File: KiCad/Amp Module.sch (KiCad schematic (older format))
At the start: 59 parts, among them J1 IDC34, J2 IDC34, J3 IDC34, Q1 S9012, Q2 S9012, Q3 S9012, Q4 S9012, SW1 SPDT, SW2 SPDT, U1 74LS08, U2 74LS08, U3 CD4053B, U4 LM393, U5 LM393, U6 LM393, U7 LM393, U8 LM393

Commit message: first 2way commit
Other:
- note added: "v2"
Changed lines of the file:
@@
 Wire Wire Line
 	8650 4700 8500 4700
+Text Notes 7650 6200 0    50   ~ 0
+v2
 $EndSCHEMATC

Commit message: added basic filter and trim
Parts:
- removed R1, R11, R3, R9: ?, symbol Device:R_Small
- removed R12, R13, R4, R5: 12k, symbol Device:R_Small
- removed RV1, RV2: 100k, symbol Device:R_POT_Dual
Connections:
- wire segments 215 -> 185
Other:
- note removed: "VOLUME CONTROL"
- note removed: "v2"

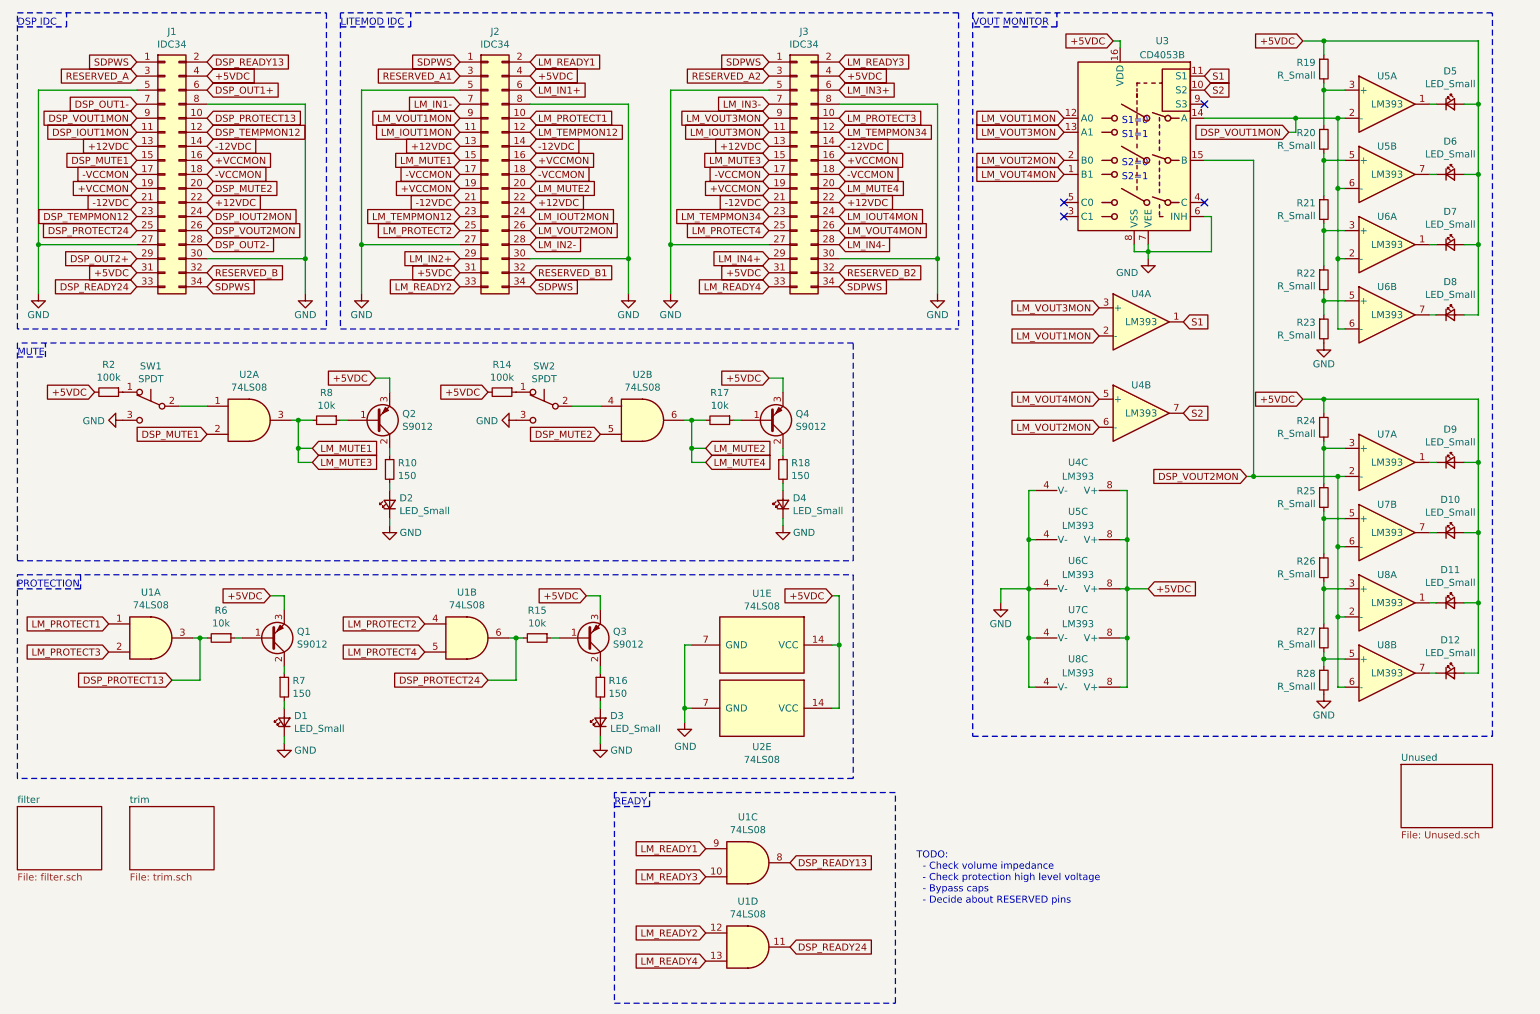
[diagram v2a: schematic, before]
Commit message: restored filter and added initial attenuation in trim
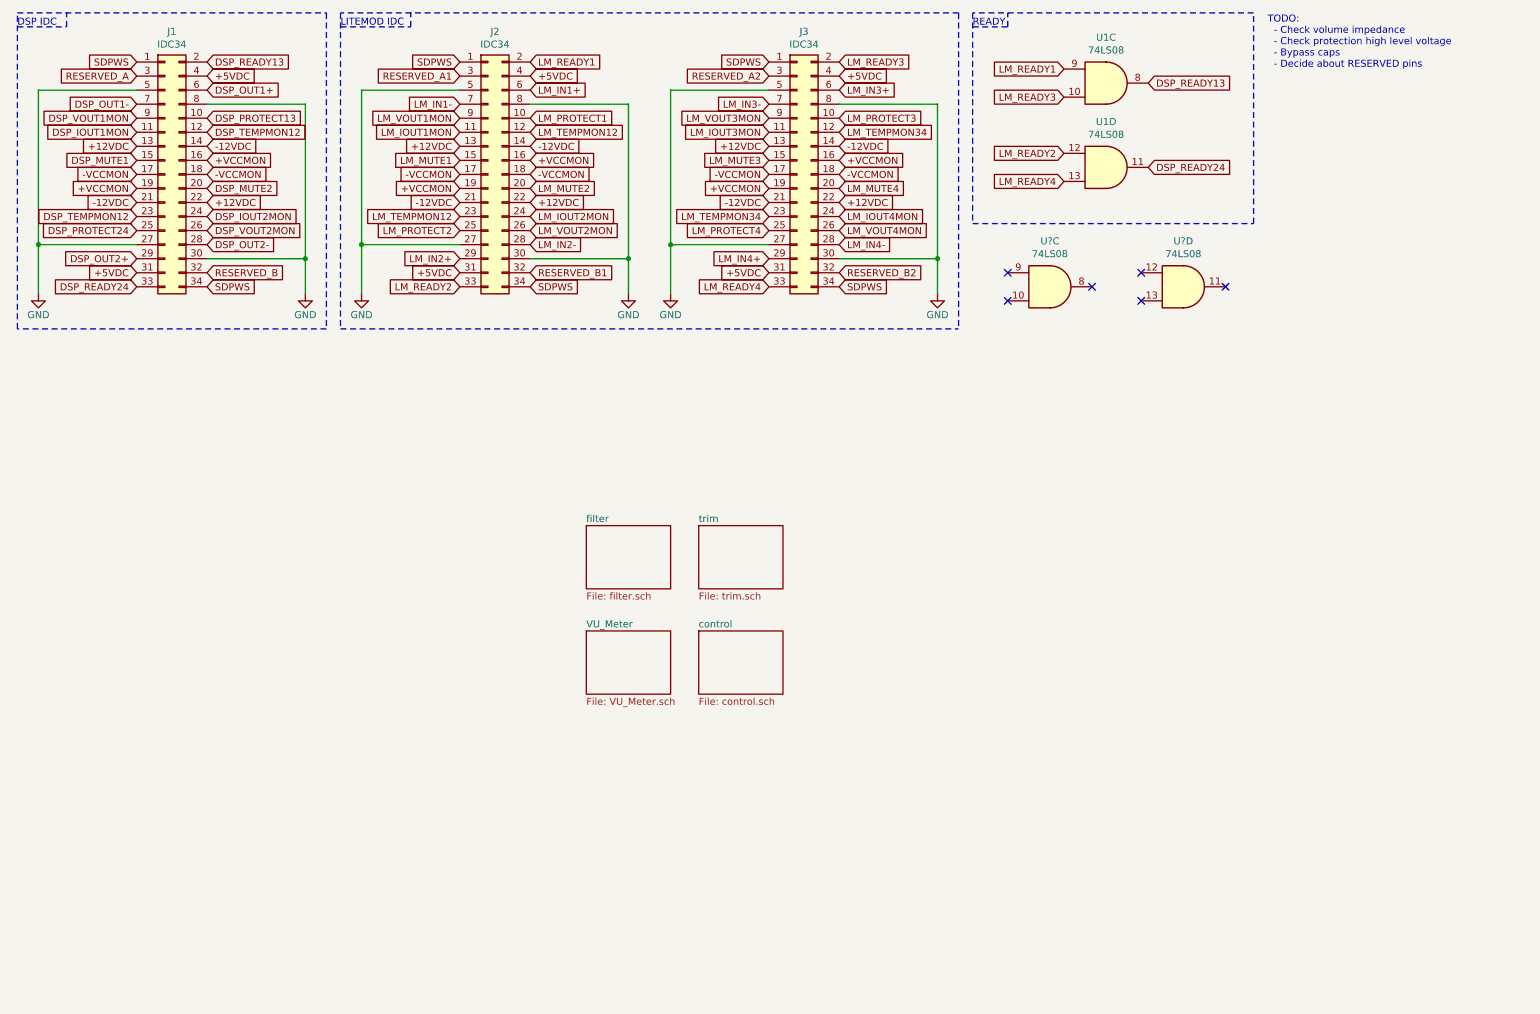
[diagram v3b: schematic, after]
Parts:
- removed D1, D10, D11, D12, D2, D3, D4, D5, D6, D7, D8, D9: LED_Small, symbol Device:LED_Small
- removed Q1, Q2, Q3, Q4: S9012, symbol Device:Q_PNP_BCE
- removed R10, R16, R18, R7: 150, symbol Device:R_Small
- removed R14, R2: 100k, symbol Device:R_Small
- removed R15, R17, R6, R8: 10k, symbol Device:R_Small
- removed R19, R20, R21, R22, R23, R24, R25, R26, R27, R28: R_Small, symbol Device:R_Small
- removed SW1, SW2: SPDT, symbol Switch:SW_Push_SPDT
- removed unit 1 of U1
- removed unit 2 of U1
- removed unit 5 of U1
- removed U2: 74LS08, symbol 74xx:74LS08
- removed U3: CD4053B, symbol Analog_Switch:CD4053B
- removed U4, U5, U6, U7, U8: LM393, symbol Comparator:LM393
- added U? (x2): 74LS08, symbol 74xx:74LS08
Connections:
- net LM_MUTE1: no longer J3.15 (Pin_15)
- net LM_MUTE2: no longer J3.20 (Pin_20)
- new net LM_MUTE3: J3.15 (Pin_15)
- new net LM_MUTE4: J3.20 (Pin_20)
- no-connect marks 4 -> 6
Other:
- note removed: "MUTE"
- note removed: "PROTECTION"
- note removed: "S1=0"
- note removed: "S1=1"
- note removed: "S2=0"
- note removed: "S2=1"
- note removed: "VOUT MONITOR"
- moved on the sheet: U1C, U1D

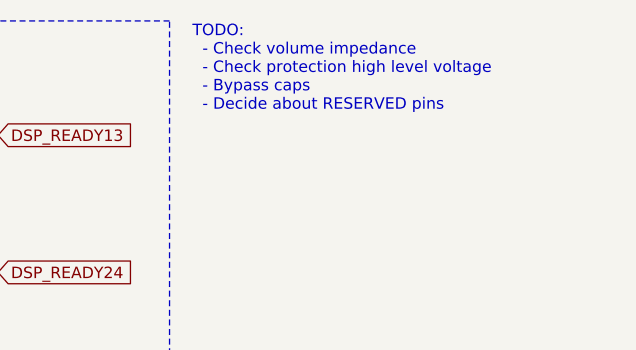
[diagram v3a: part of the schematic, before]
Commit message: changed Q to a fixed value
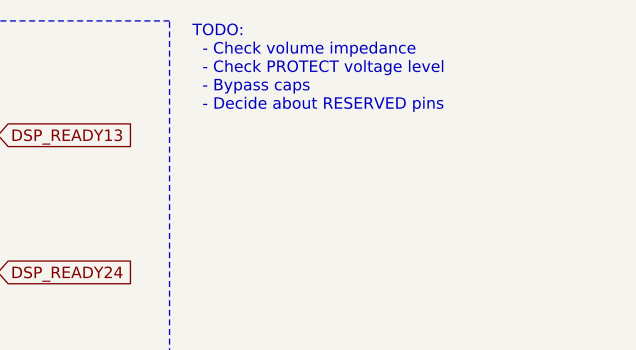
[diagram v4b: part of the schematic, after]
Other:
- note added: "TODO:\n - Check volume impedance\n - Check PROTECT voltage level\n - Bypass caps\n - Decide about RESERVED pins"
- note removed: "TODO:\n - Check volume impedance\n - Check protection high level voltage\n - Bypass caps\n - Decide about RESERVED pins"
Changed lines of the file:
@@
 $EndComp
 Text Notes 9500 1000 0    50   ~ 0
-TODO:\n  - Check volume impedance\n  - Check protection high level voltage\n  - Bypass caps\n  - Decide about RESERVED pins
+TODO:\n  - Check volume impedance\n  - Check PROTECT voltage level\n  - Bypass caps\n  - Decide about RESERVED pins
 Wire Notes Line
 	7400 600  7400 2100

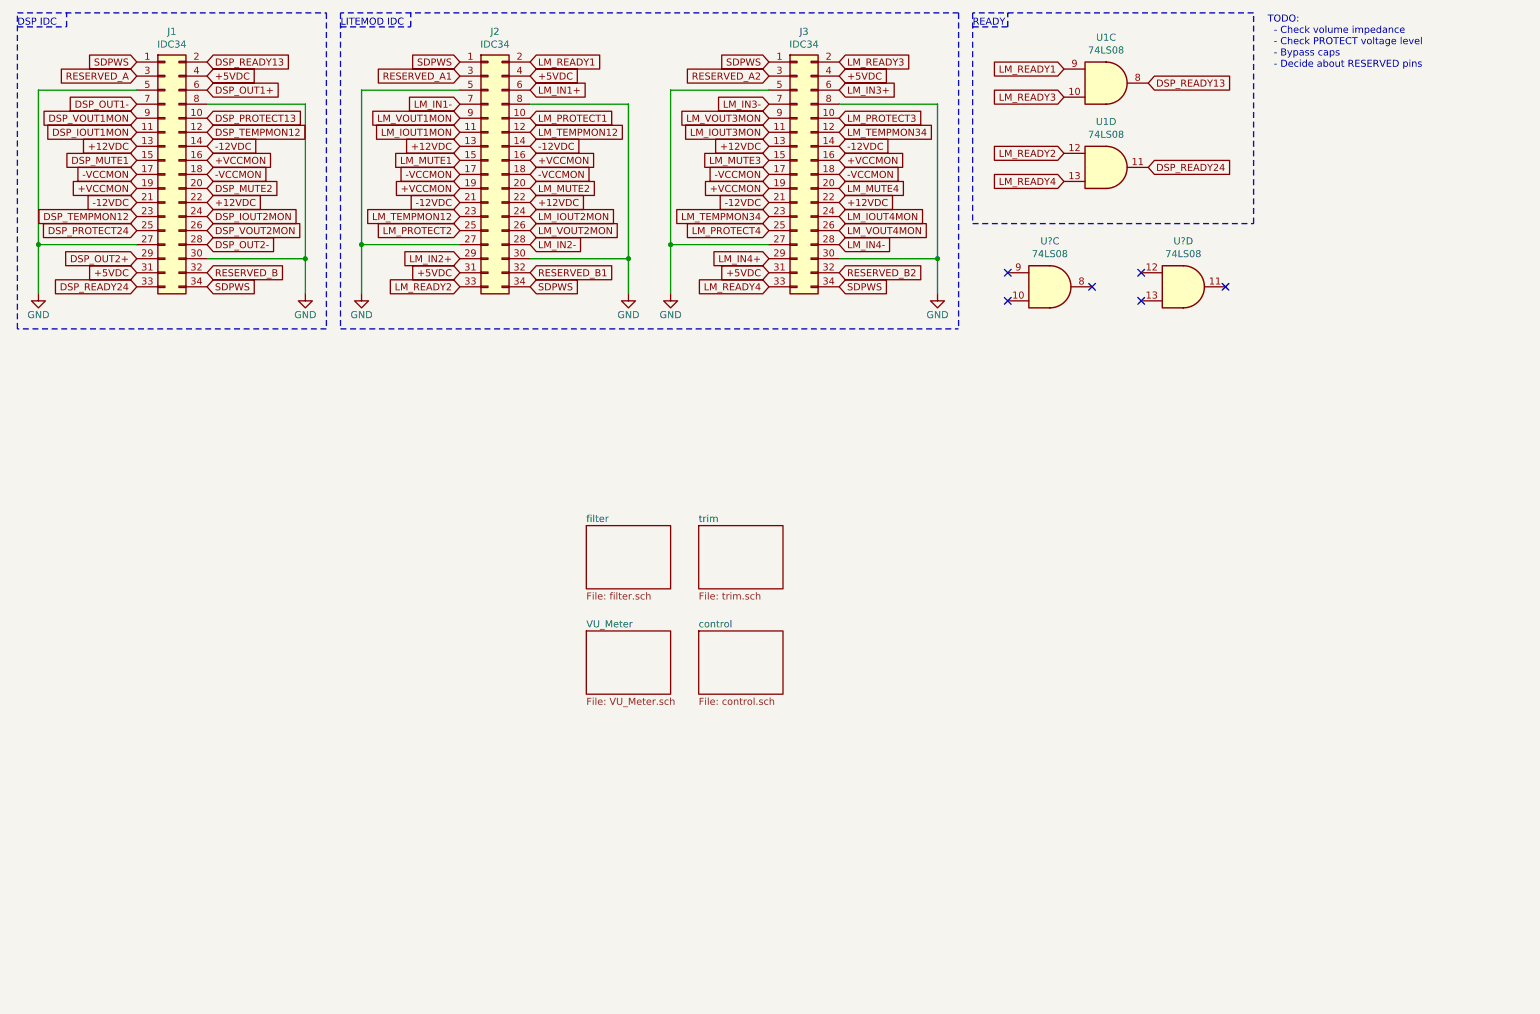
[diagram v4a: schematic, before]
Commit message: removed VU Meter sheet
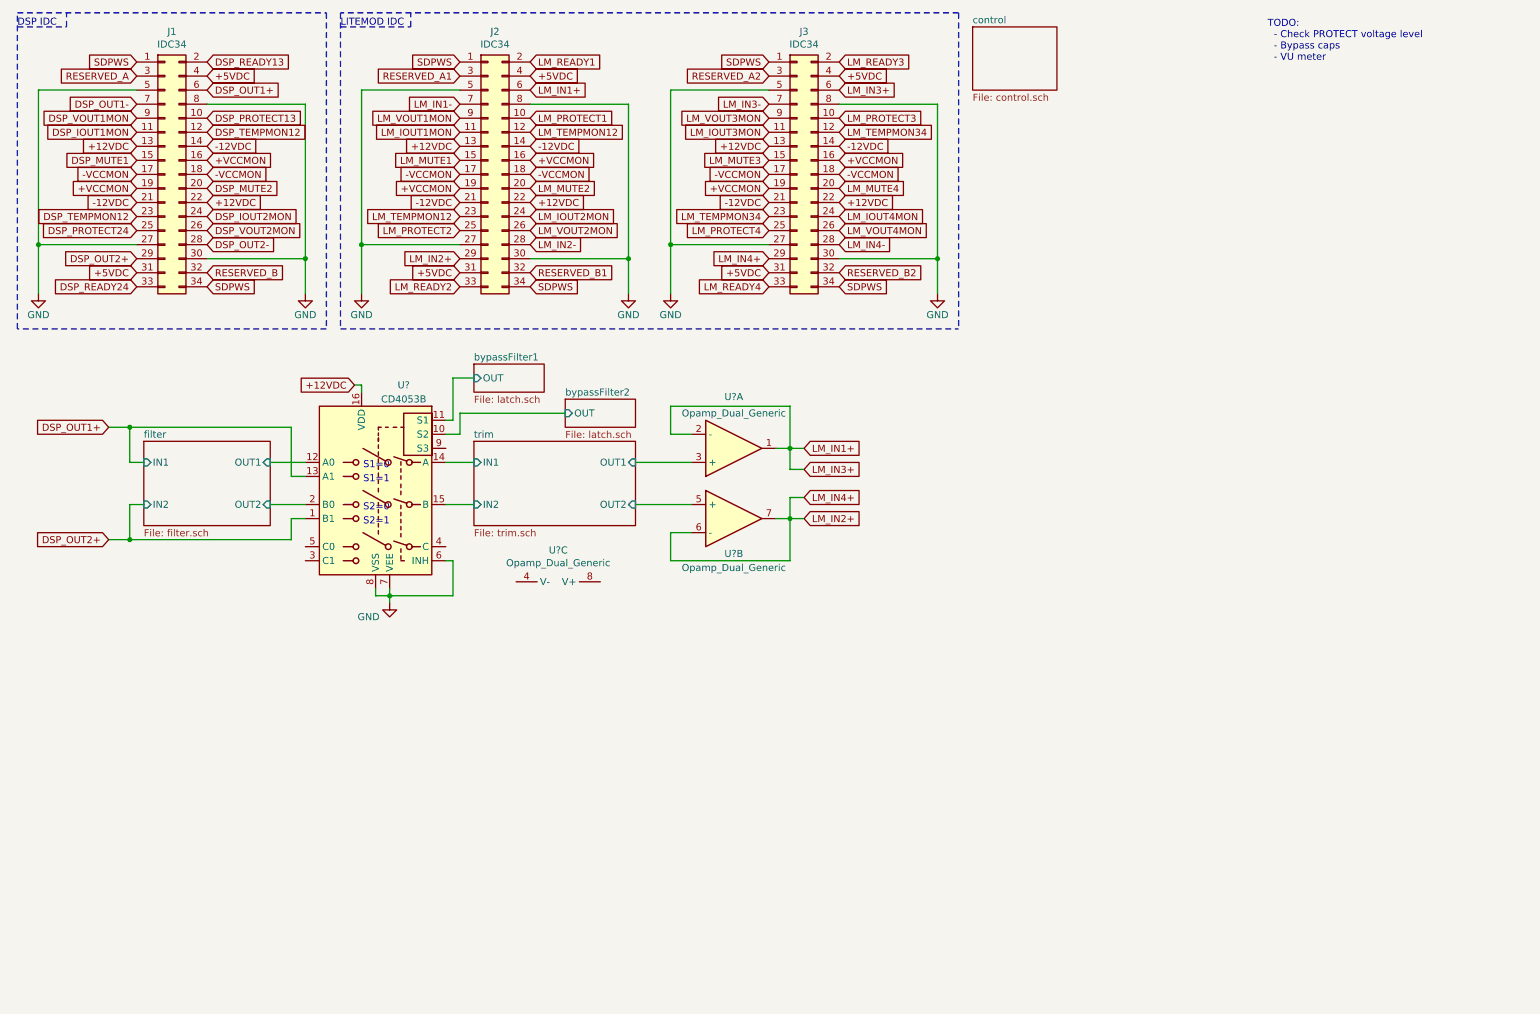
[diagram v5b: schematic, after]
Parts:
- removed U1, U? (x2): 74LS08, symbol 74xx:74LS08
- added U? (x3): Opamp_Dual_Generic, symbol Device:Opamp_Dual_Generic
- added U?: CD4053B, symbol Analog_Switch:CD4053B
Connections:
- net LM_IN3+ is gone; now on net LM_IN1+: J3.6 (Pin_6)
- net LM_IN4+ is gone; now on net LM_IN2+: J3.29 (Pin_29)
- net +12VDC: now also U?.16 (VDD)
- net DSP_OUT1+: now also U?.13 (A1)
- net DSP_OUT2+: now also U?.1 (B1)
- net GND: now also U?.6 (INH), U?.7 (VEE), U?.8 (VSS)
- net LM_IN1+: now also U?.1, U?.2 (-)
- net LM_IN2+: now also U?.6 (-), U?.7
- new net bypassFilter1/OUT: U?.11 (S1)
- new net bypassFilter2/OUT: U?.10 (S2)
- new net filter/OUT1: U?.12 (A0)
- new net filter/OUT2: U?.2 (B0)
- new net trim/IN1: U?.14 (A)
- new net trim/IN2: U?.15 (B)
- new net trim/OUT1: U?.3 (+)
- new net trim/OUT2: U?.5 (+)
- no-connect marks 6 -> 0
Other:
- note added: "S1=0"
- note added: "S1=1"
- note added: "S2=0"
- note added: "S2=1"
- note added: "TODO:\n - Check PROTECT voltage level\n - Bypass caps\n - VU meter"
- note removed: "READY"
- note removed: "TODO:\n - Check volume impedance\n - Check PROTECT voltage level\n - Bypass caps\n - Decide about RESERVED pins"
